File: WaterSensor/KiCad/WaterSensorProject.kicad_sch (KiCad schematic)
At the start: 17 parts, among them Q1_A1 TEPT4400, Q1_B1 TEPT4400, U1 TLV7042DDFR, U2 ESP32-C3, U3 RP604K331A-TR

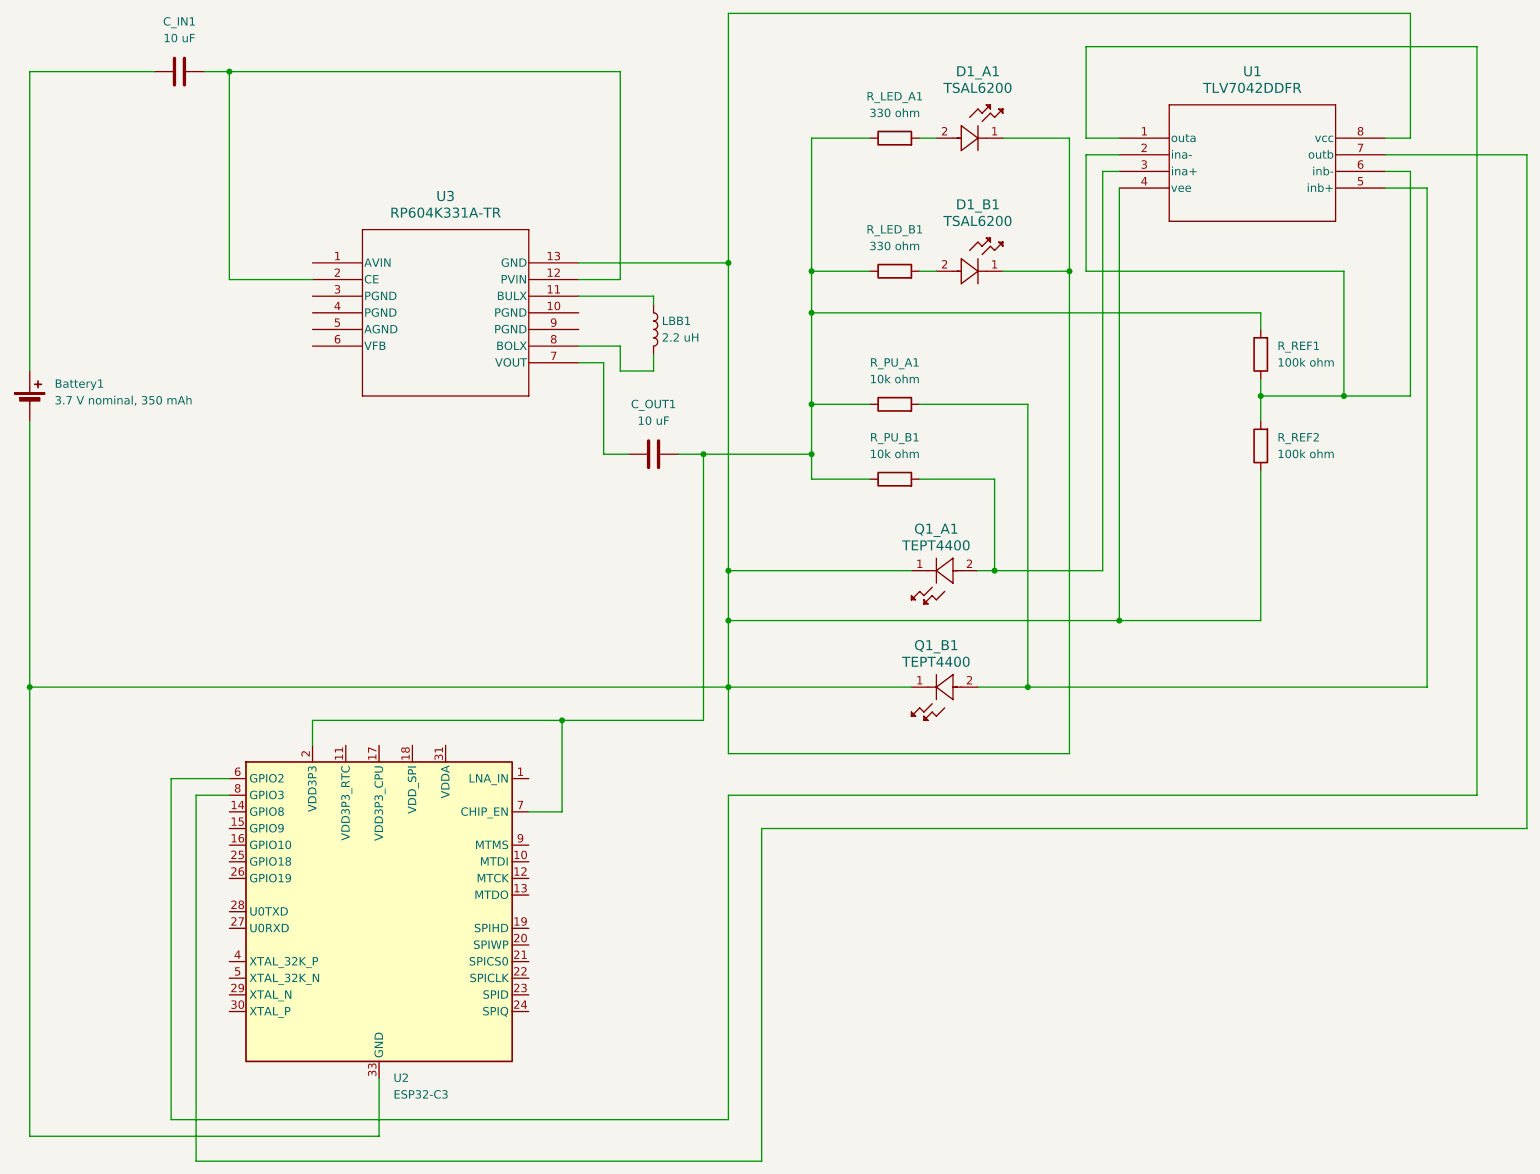
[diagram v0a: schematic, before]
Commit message: Updated schematic, created 2 pcbs with tracks, proper footprints & models
- Updated schematic
- Downloaded, imported all correct footprints and models
- Created 2 viable PCBs with tracks
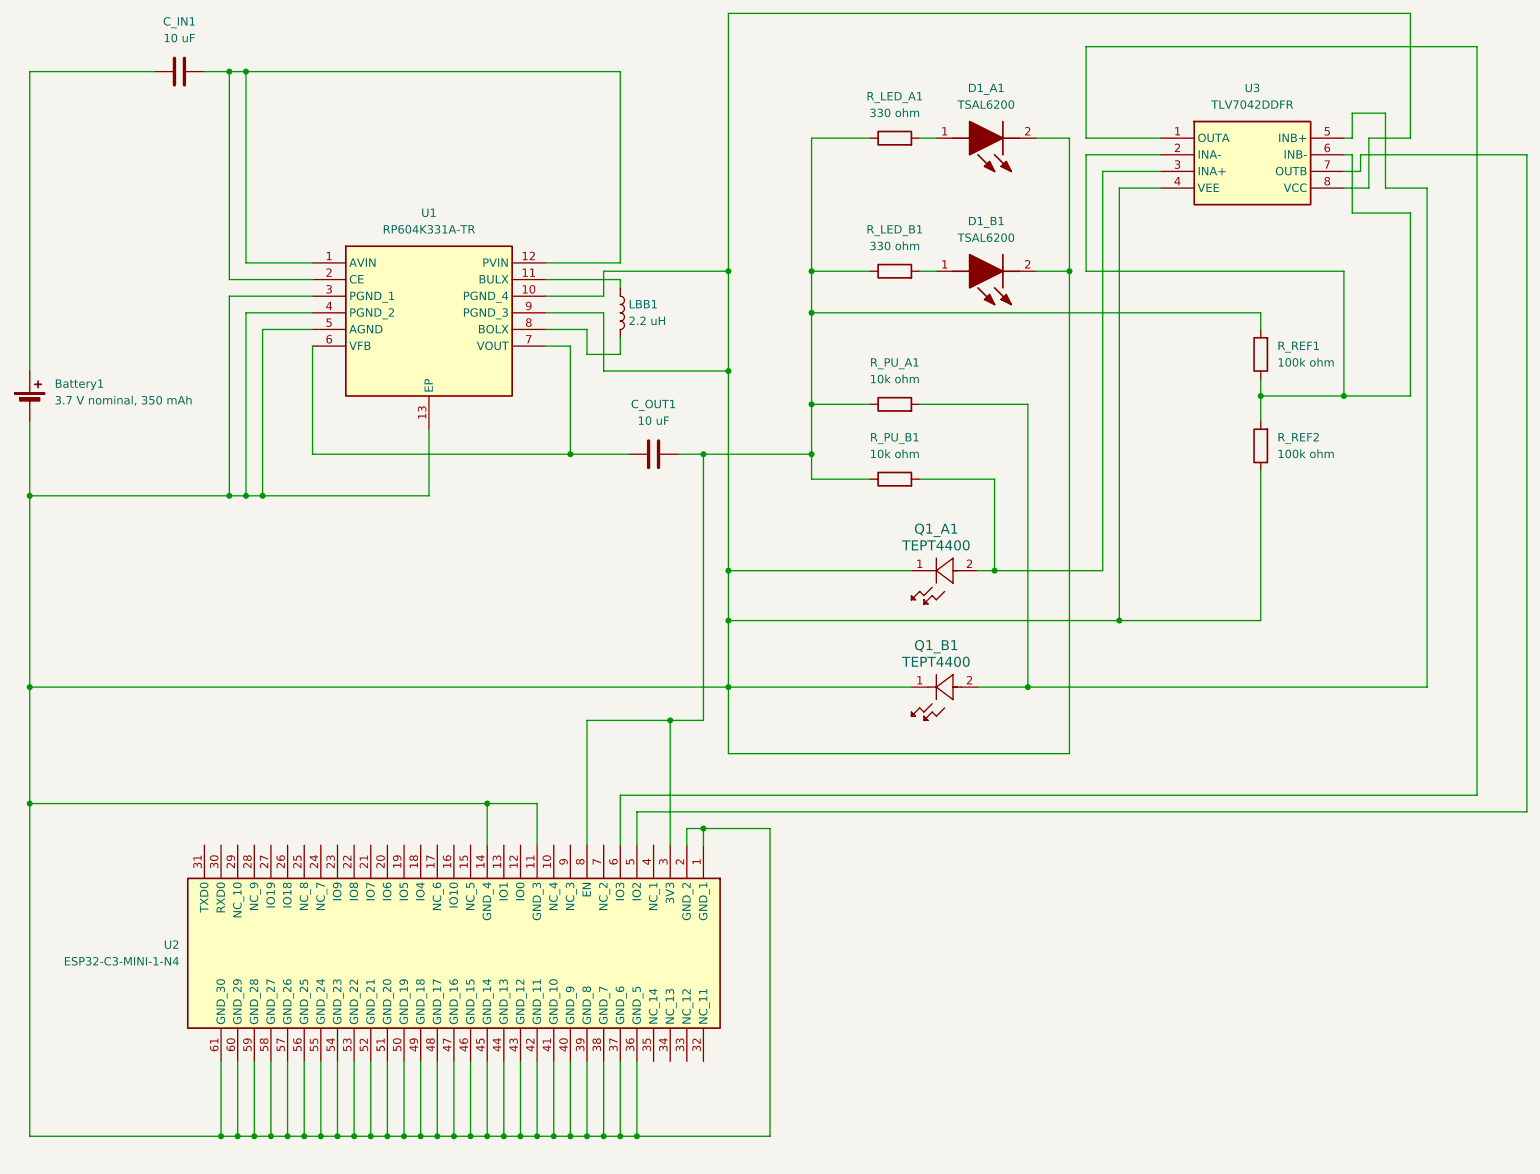
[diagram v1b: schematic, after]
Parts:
- removed D1_A1, D1_B1: TSAL6200, Diode_THT:D_5KPW_P7.62mm_Vertical_AnodeUp, symbol 2025-01-17_05-16-59:TSAL6200
- removed U1: TLV7042DDFR, Sensor:ASAIR_AM2302_P2.54mm_Lead2.75mm_TabDown, symbol 2025-01-17_05-18-22:TLV7042DDFR
- removed U2: ESP32-C3, Package_DFN_QFN:QFN-32-1EP_5x5mm_P0.5mm_EP3.7x3.7mm, symbol MCU_Espressif:ESP32-C3
- removed U3: RP604K331A-TR, Sensor:ASAIR_AM2302_P2.54mm_Lead2.75mm_TabDown, symbol RP604K331A:RP604K331A-TR
- added D1_A1, D1_B1: TSAL6200, TSAL6200:TSAL6200, symbol TSAL6200:TSAL6200
- added U1: RP604K331A-TR, RP604K331A-TR:SON50P270X300X60-13N, symbol RP604K331A-TR:RP604K331A-TR
- added U2: ESP32-C3-MINI-1-N4, ESP32-C3-MINI-1-N4:ESP32C3MINI1N4, symbol ESP32-C3-MINI-1-N4:ESP32-C3-MINI-1-N4
- added U3: TLV7042DDFR, TLV7042DDFR:SOT65P280X110-8N, symbol TLV7042DDFR:TLV7042DDFR
- Battery1: footprint Battery:BatteryClip_Keystone_54_D16-19mm -> Battery:BatteryHolder_Keystone_2466_1xAAA
- Q1_A1, Q1_B1: footprint Diode_SMD:D_0201_0603Metric -> TEPT4400:LED_TEPT4400_VIS
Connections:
- net at R_REF1.1, R_REF2.2: now also U3.2 (INA-), U3.6 (INB-)
- net at Q1_A1.2, R_PU_B1.2: now also U3.3 (INA+)
- net at Battery1.2 (-), Q1_A1.1, Q1_B1.1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: now also D1_A1.2 (K), D1_B1.2 (K), U1.10 (PGND_4), U1.13 (EP), U1.3 (PGND_1), U1.4 (PGND_2), U1.5 (AGND), U1.9 (PGND_3), U2.1 (GND_1), U2.11 (GND_3), U2.14 (GND_4), U2.2 (GND_2), U2.36 (GND_5), U2.37 (GND_6), U2.38 (GND_7), U2.39 (GND_8), U2.40 (GND_9), U2.41 (GND_10), U2.42 (GND_11), U2.43 (GND_12), U2.44 (GND_13), U2.45 (GND_14), U2.46 (GND_15), U2.47 (GND_16), U2.48 (GND_17), U2.49 (GND_18), U2.50 (GND_19), U2.51 (GND_20), U2.52 (GND_21), U2.53 (GND_22), U2.54 (GND_23), U2.55 (GND_24), U2.56 (GND_25), U2.57 (GND_26), U2.58 (GND_27), U2.59 (GND_28), U2.60 (GND_29), U2.61 (GND_30), U3.4 (VEE), U3.8 (VCC)
- net at Q1_B1.2, R_PU_A1.2: now also U3.5 (INB+)
- net at C_OUT1.2, R_LED_A1.1, R_LED_B1.1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: now also U2.3 (3V3), U2.8 (EN)
- net at C_IN1.2: now also U1.1 (AVIN), U1.12 (PVIN), U1.2 (CE)
- net at LBB1.1: now also U1.11 (BULX)
- net at LBB1.2: now also U1.8 (BOLX)
- net at C_OUT1.1: now also U1.6 (VFB), U1.7 (VOUT)
- net at R_LED_B1.2: now also D1_B1.1 (A)
- net at R_LED_A1.2: now also D1_A1.1 (A)
- new net: U2.5 (IO2), U3.7 (OUTB)
- new net: U2.6 (IO3), U3.1 (OUTA)
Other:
- company: (none) -> Billy Miller
- title: (none) -> WaterSensorCircuit
- moved on the sheet: LBB1
